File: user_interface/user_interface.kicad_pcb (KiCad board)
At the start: 2 copper layers, 12 parts, among them J1 Conn_01x06, U1 ADS1115IDGS, U2 ADS1115IDGS, U3 TXS0101DCKR

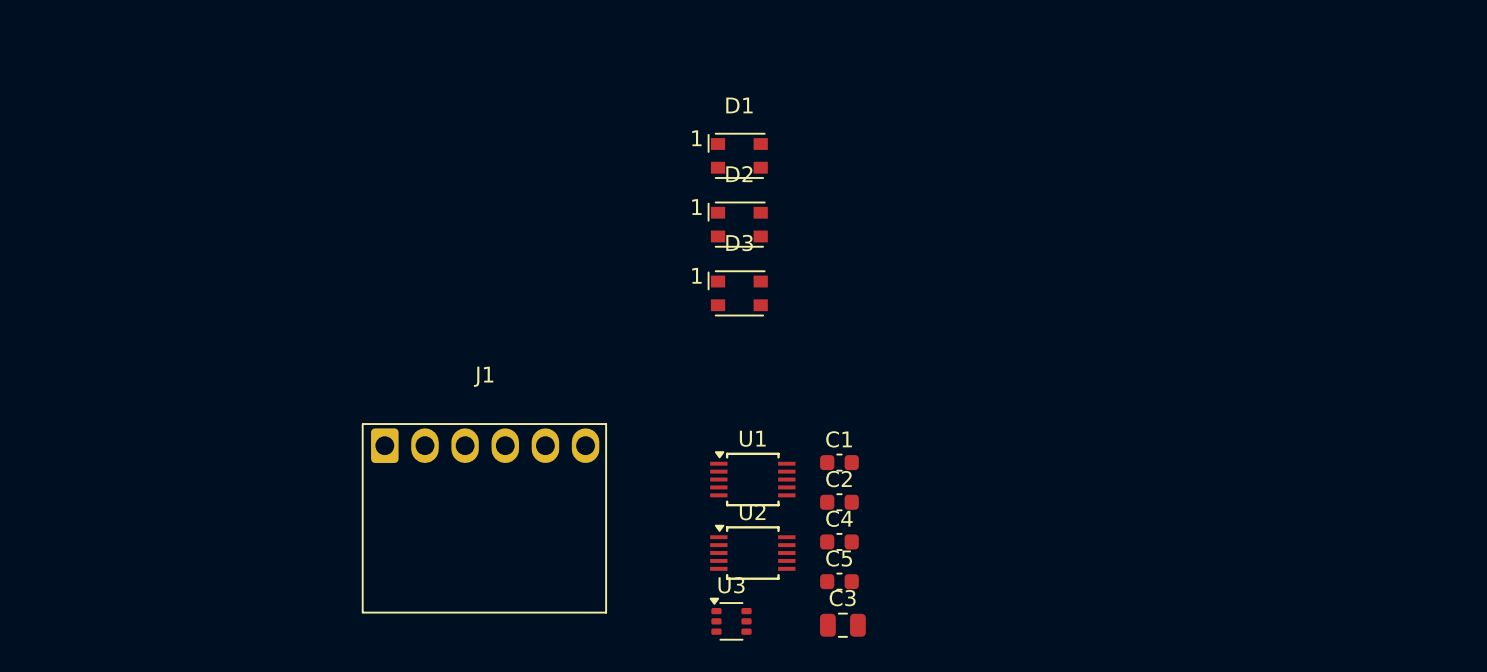
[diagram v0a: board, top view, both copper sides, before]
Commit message: Mostly finished the User Interface PCB
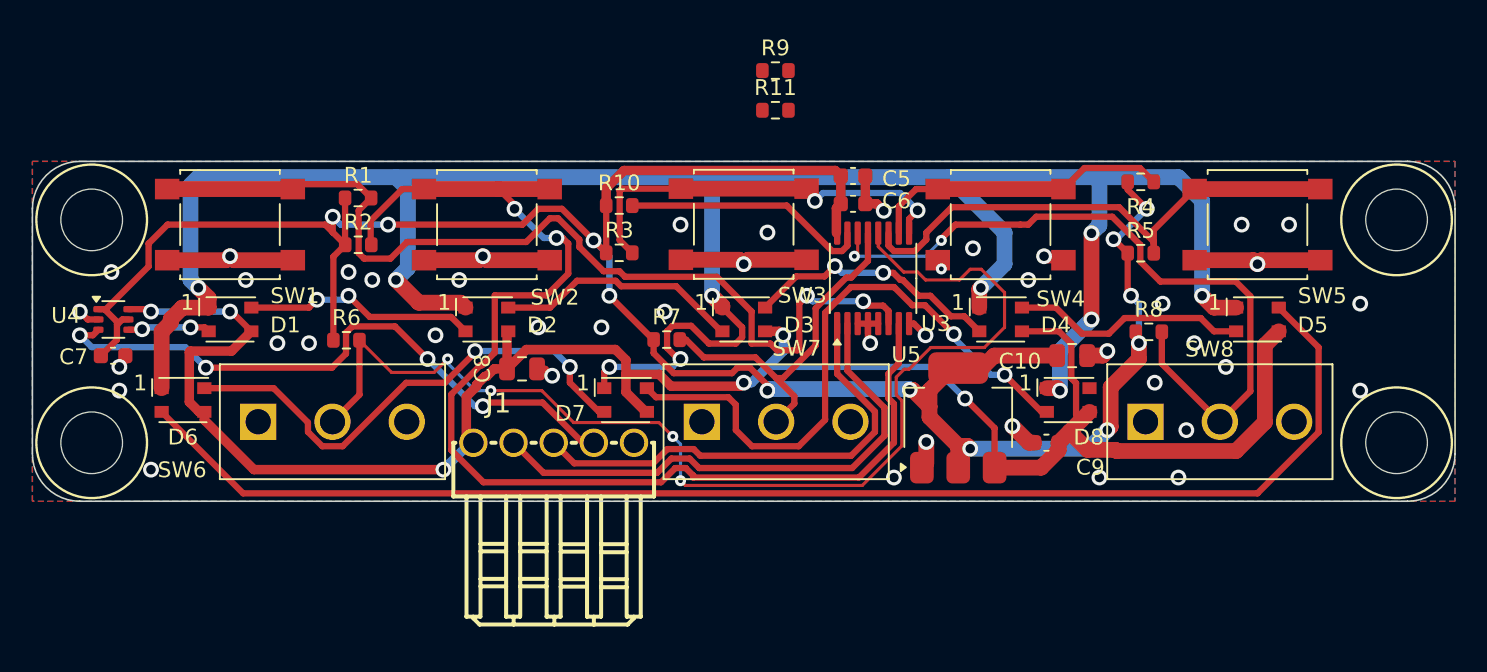
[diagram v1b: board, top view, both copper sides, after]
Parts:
- removed C1, C2: 1u, Capacitor_SMD:C_0603_1608Metric
- removed C3: 10u, Capacitor_SMD:C_0805_2012Metric
- removed C4: 100n, Capacitor_SMD:C_0603_1608Metric
- removed U1, U2: ADS1115IDGS, Package_SO:TSSOP-10_3x3mm_P0.5mm
- added C10: 10u, Capacitor_SMD:C_0805_2012Metric, F.Cu at (156.3, 97.3)
- added C6: 100n, Capacitor_SMD:C_0603_1608Metric, F.Cu at (142.4, 87.7)
- added C7: 100n, Capacitor_SMD:C_0603_1608Metric, F.Cu at (95.6, 97.3)
- added C8: 10u, Capacitor_SMD:C_0805_2012Metric, F.Cu at (121.5, 98.1)
- added C9: 1u, Capacitor_SMD:C_0603_1608Metric, F.Cu at (154.6, 102.8)
- added D4: WS2812B, RP2040_minimal:LED_WS2812_3528_3.5x2.8mm_P1.5mm, F.Cu at (151.8, 95.0)
- added D5: WS2812B, RP2040_minimal:LED_WS2812_3528_3.5x2.8mm_P1.5mm, F.Cu at (168.0, 95.0)
- added D6: WS2812B, RP2040_minimal:LED_WS2812_3528_3.5x2.8mm_P1.5mm, F.Cu at (100.0, 100.1)
- added D7: WS2812B, RP2040_minimal:LED_WS2812_3528_3.5x2.8mm_P1.5mm, F.Cu at (128.0, 100.1)
- added D8: WS2812B, RP2040_minimal:LED_WS2812_3528_3.5x2.8mm_P1.5mm, F.Cu at (156.0, 100.1)
- added H1: MountingHole, RP2040_minimal:MountingHole_3.9mm_Plastite_#6, F.Cu at (94.2, 88.7)
- added H2: MountingHole, RP2040_minimal:MountingHole_3.9mm_Plastite_#6, F.Cu at (94.2, 102.8)
- added H3: MountingHole, RP2040_minimal:MountingHole_3.9mm_Plastite_#6, F.Cu at (176.8, 88.7)
- added H4: MountingHole, RP2040_minimal:MountingHole_3.9mm_Plastite_#6, F.Cu at (176.8, 102.8)
- added R1: 10k, Resistor_SMD:R_0603_1608Metric, F.Cu at (111.1, 87.3)
- added R10: 10k, Resistor_SMD:R_0603_1608Metric, F.Cu at (127.6, 87.8)
- added R11: 10k, Resistor_SMD:R_0603_1608Metric, F.Cu at (137.5, 81.8)
- added R2: 10k, Resistor_SMD:R_0603_1608Metric, F.Cu at (111.1, 90.3)
- added R3: 10k, Resistor_SMD:R_0603_1608Metric, F.Cu at (127.6, 90.8)
- added R4: 10k, Resistor_SMD:R_0603_1608Metric, F.Cu at (160.6, 86.3)
- added R5: 10k, Resistor_SMD:R_0603_1608Metric, F.Cu at (160.6, 90.8)
- added R6: 10k, Resistor_SMD:R_0603_1608Metric, F.Cu at (110.4, 96.3)
- added R7: 10k, Resistor_SMD:R_0603_1608Metric, F.Cu at (130.6, 96.3)
- added R8: 10k, Resistor_SMD:R_0603_1608Metric, F.Cu at (161.1, 95.8)
- added R9: 10k, Resistor_SMD:R_0603_1608Metric, F.Cu at (137.5, 79.3)
- added SW1: SW_SPST, Button_Switch_SMD:SW_SPST_B3S-1000, F.Cu at (103.0, 89.0)
- added SW2: SW_SPST, Button_Switch_SMD:SW_SPST_B3S-1000, F.Cu at (119.2, 89.0)
- added SW3: SW_SPST, Button_Switch_SMD:SW_SPST_B3S-1000, F.Cu at (135.5, 89.0)
- added SW4: SW_SPST, Button_Switch_SMD:SW_SPST_B3S-1000, F.Cu at (151.8, 89.0)
- added SW5: SW_SPST, Button_Switch_SMD:SW_SPST_B3S-1000, F.Cu at (168.0, 89.0)
- added SW6: SW_SPDT, parts:CS12ANW03, F.Cu at (104.8, 101.5)
- added SW7: SW_SPDT, parts:CS12ANW03, F.Cu at (132.9, 101.5)
- added SW8: SW_SPDT, parts:CS12ANW03, F.Cu at (160.9, 101.5)
- added U4: TXS0101DCKR, Package_TO_SOT_SMD:SOT-363_SC-70-6, F.Cu at (95.6, 95.0)
- added U5: TLV1117LV33DCYR, Package_TO_SOT_SMD:SOT-223-3_TabPin2, F.Cu at (149.1, 101.2)
- C5: value 100n -> 1u
- J1: value Conn_01x06 -> AUX Encoder; footprint parts:Ckmtw-W-2510S06P_1x06_P2.54mm_Horizontal -> parts:CONN-TH_5P-P2.54_HCTL_HC-2510-5AW
- U3: value TXS0101DCKR -> PCA9557PW; footprint Package_TO_SOT_SMD:SOT-363_SC-70-6 -> Package_SO:TSSOP-16_4.4x5mm_P0.65mm
- moved D1 33.8 mm to (103.0, 95.0)
- moved C5 25.7 mm to (142.4, 85.9), turned to 180 degrees
- moved U3 23.5 mm to (143.7, 92.4), turned to 90 degrees
- moved D2 17.1 mm to (119.2, 95.0)
- moved J1 10.7 mm to (123.5, 102.8)
- moved D3 1.67 mm to (135.5, 95.0)
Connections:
- C5 pad 1: +3V3 -> GND
- C5 pad 2: GND -> +3V3
- D3 pad 4: unconnected-(D3-DOUT-Pad4) -> Net-(D3-DOUT)
- J1 pad 1: unconnected-(J1-Pin_1-Pad1) -> +5V
- J1 pad 2: +3V3 -> SDA
- J1 pad 3: SDA -> SCL
- J1 pad 4: SCL -> LED
- J1 pad 5: LED -> GND
- U3 pad 1: +3V3 -> SCL
- U3 pad 2: GND -> SDA
- U3 pad 3: LED -> GND
- U3 pad 4: Net-(D1-DIN) -> GND
- U3 pad 5: +3V3 -> GND
- U3 pad 6: +5V -> /SW1
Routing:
- net /WS2812_SINK: track 0.00 -> 152.1 mm, vias 0 -> 10
- net +3V3: track 0.00 -> 148.7 mm, vias 0 -> 12
- net +5V: track 0.00 -> 125.7 mm, vias 0 -> 6
- net Net-(D5-DOUT): track 0.00 -> 85.9 mm
- net /SW2: track 0.00 -> 76.2 mm, vias 0 -> 2
- net /SW6: track 0.00 -> 72.7 mm, vias 0 -> 4
- net /SW1: track 0.00 -> 61.1 mm, vias 0 -> 2
- net GND: track 0.00 -> 50.0 mm, vias 0 -> 44
- net /SW8: track 0.00 -> 46.3 mm, vias 0 -> 2
- net LED: track 0.00 -> 39.8 mm, vias 0 -> 4
- net Net-(D7-DOUT): track 0.00 -> 39.3 mm, vias 0 -> 2
- net /SW5: track 0.00 -> 33.8 mm
- net SDA: track 0.00 -> 33.8 mm
- net Net-(D6-DOUT): track 0.00 -> 31.9 mm, vias 0 -> 2
- net SCL: track 0.00 -> 29.9 mm
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- added copper zone on B.Cu, net GND
- added copper zone on F.Cu, net GND
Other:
- board outline added: 90 x 21.5 mm

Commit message: Update user_interface pcb
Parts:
- added G***: LOGO, taylor_footprints:twisted_2, B.Cu at (154.3, 90.0)
- added G***: LOGO, taylor_footprints:twisted_icon, B.Cu at (169.5, 88.9)
- added G***: LOGO, taylor_footprints:twisted, B.Cu at (157.7, 90.0)
- moved R9 21.0 mm to (126.1, 96.9)
- moved R11 17.7 mm to (126.1, 95.3)
- moved C7 2.71 mm to (98.3, 97.1)
- moved U4 2.71 mm to (98.3, 94.8)
- moved C9 1.57 mm to (153.2, 103.5), turned to 90 degrees
- moved R7 0.85 mm to (130.3, 95.5)
- moved U5 0.30 mm to (148.8, 101.2)
- moved C10 0.20 mm to (156.3, 97.1)
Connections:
- D1 pad 1: /WS2812_SINK -> GND
- D2 pad 1: /WS2812_SINK -> GND
- D3 pad 1: /WS2812_SINK -> GND
- D4 pad 1: /WS2812_SINK -> GND
- D5 pad 1: /WS2812_SINK -> GND
- D6 pad 1: /WS2812_SINK -> GND
- D7 pad 1: /WS2812_SINK -> GND
- D8 pad 1: /WS2812_SINK -> GND
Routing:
- net /WS2812_SINK: track 152.1 -> 0.00 mm, vias 10 -> 0
- net /SW2: track 76.2 -> 50.6 mm, vias 2 -> 3
- net GND: track 50.0 -> 32.1 mm, vias 44 -> 27
- net /SW8: track 46.3 -> 32.3 mm, vias 2 -> 3
- net /SW6: track 72.7 -> 59.0 mm, vias 4 -> 0
- net +3V3: track 148.7 -> 140.0 mm, vias 12 -> 8
- net Net-(D7-DOUT): track 39.3 -> 31.4 mm
- net LED: track 39.8 -> 32.7 mm, vias 4 -> 1
- net /SW1: track 61.1 -> 54.4 mm
- net Net-(U3-~{RESET}): track 15.7 -> 20.9 mm
- net SDA: track 33.8 -> 38.9 mm
- net Net-(D5-DOUT): track 85.9 -> 82.6 mm, vias 0 -> 2
- net Net-(D6-DOUT): track 31.9 -> 29.3 mm
- net Net-(D1-DIN): track 5.24 -> 2.64 mm, vias 2 -> 0
- net SCL: track 29.9 -> 32.4 mm
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- added copper zone on In1.Cu, net GND
- added copper zone on In2.Cu, net GND
- removed copper zone on B.Cu, net GND
- removed copper zone on F.Cu, net GND
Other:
- copper layers 2 -> 4
- board text added: "1"
- board text added: "2"
- board text added: "3"
- board text added: "4"
- board text added: "5"
- board text added: "6"
- board text added: "7"
- board text added: "8"
- board text added: "Be Kind"
- board text added: "Corner Interface PCB V1"
- board text added: "Designed by Sequoia Sempervirens"
- board text added: "I'm glad you're here. <3"
- board text added: "Love everyone."
- board text added: "github.com/Twisted-Fields/rp2040-motor-controller/user_interface"

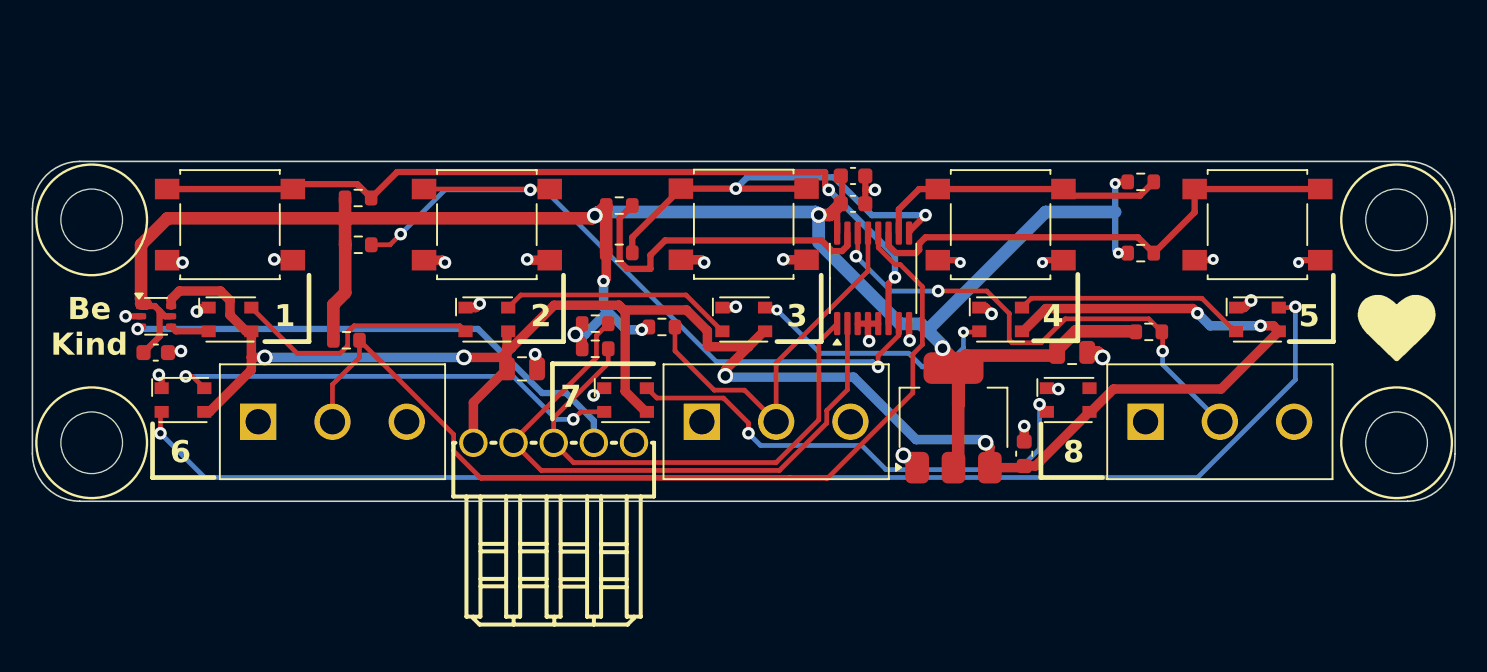
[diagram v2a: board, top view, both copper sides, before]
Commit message: Clean up of motor, base, and UI PCBs. Could be ready to order.
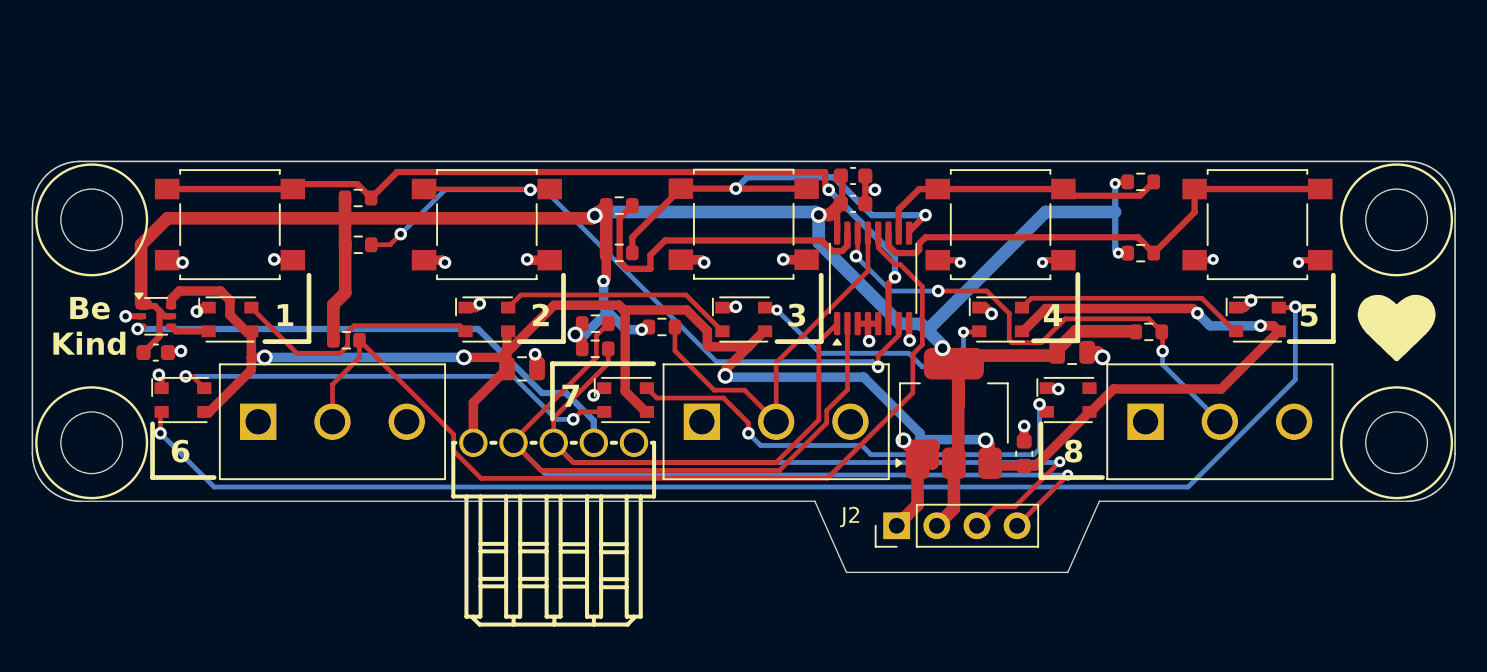
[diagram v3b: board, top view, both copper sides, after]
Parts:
- added J2: I2C OLED, Connector_PinHeader_2.54mm:PinHeader_1x04_P2.54mm_Vertical, F.Cu at (145.2, 108.0)
- moved U5 0.28 mm to (148.8, 101.0)
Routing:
- net SDA: track 38.9 -> 79.3 mm, vias 0 -> 1
- net SCL: track 32.4 -> 71.8 mm, vias 0 -> 1
- net GND: track 32.1 -> 39.5 mm
- net +3V3: track 140.0 -> 144.3 mm
- net Net-(D7-DOUT): track 31.4 -> 30.6 mm
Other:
- board size 90 x 21.5 mm -> 90 x 26 mm
